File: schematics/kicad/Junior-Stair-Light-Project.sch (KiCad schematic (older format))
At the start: 72 parts, among them J1 12V Eingang, J2 LED_stripes_per_step, T1_1 BC337, T1_10 BC327, T1_11 BC337, T1_12 BC337, T1_13 BC337, T1_14 BC337, T1_15 BC337, T1_16 BC327, T1_17 BC327, T1_18 BC327, T1_19 BC327, T1_2 BC327, T1_20 BC327, T1_21 BC337, T1_22 BC337, T1_23 BC337, T1_24 BC327, T1_25 BC327, T1_26 BC327, T1_3 BC337, T1_4 BC337, T1_5 BC337, T1_6 BC337, T1_7 BC327, T1_8 BC327, T1_9 BC327, U1 7805, U2 Arduino_Nano

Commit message: First edition of PCB done
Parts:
- removed U1: 7805, symbol 7805
- added U1: L4940V5, TO_SOT_Packages_THT:TO-220_Vertical, symbol L4940V5
- C1, C2: footprint (none) -> Capacitors_THT:CP_Radial_D7.5mm_P2.50mm
- C3: footprint (none) -> Capacitors_THT:C_Disc_D3.8mm_W2.6mm_P2.50mm
- J1: footprint (none) -> Connectors_JST:JST_XH_B02B-XH-A_02x2.50mm_Straight
- J2: footprint (none) -> Connectors_JST:JST_XH_B15B-XH-A_15x2.50mm_Straight
- R10_1: renamed from R1_10; footprint (none) -> Resistors_THT:R_Axial_DIN0207_L6.3mm_D2.5mm_P7.62mm_Horizontal
- R10_2: renamed from R20; footprint (none) -> Resistors_THT:R_Axial_DIN0207_L6.3mm_D2.5mm_P7.62mm_Horizontal
- R10_3: renamed from R19; footprint (none) -> Resistors_THT:R_Axial_DIN0207_L6.3mm_D2.5mm_P7.62mm_Horizontal
- R11_1: renamed from R1_11; footprint (none) -> Resistors_THT:R_Axial_DIN0207_L6.3mm_D2.5mm_P7.62mm_Horizontal
- R11_2: renamed from R22; footprint (none) -> Resistors_THT:R_Axial_DIN0207_L6.3mm_D2.5mm_P7.62mm_Horizontal
- R11_3: renamed from R21; footprint (none) -> Resistors_THT:R_Axial_DIN0207_L6.3mm_D2.5mm_P7.62mm_Horizontal
- R12_1: renamed from R1_12; footprint (none) -> Resistors_THT:R_Axial_DIN0207_L6.3mm_D2.5mm_P7.62mm_Horizontal
- R12_2: renamed from R24; footprint (none) -> Resistors_THT:R_Axial_DIN0207_L6.3mm_D2.5mm_P7.62mm_Horizontal
- R12_3: renamed from R23; footprint (none) -> Resistors_THT:R_Axial_DIN0207_L6.3mm_D2.5mm_P7.62mm_Horizontal
- R13_1: renamed from R1_13; footprint (none) -> Resistors_THT:R_Axial_DIN0207_L6.3mm_D2.5mm_P7.62mm_Horizontal
- R13_2: renamed from R26; footprint (none) -> Resistors_THT:R_Axial_DIN0207_L6.3mm_D2.5mm_P7.62mm_Horizontal
- R13_3: renamed from R25; footprint (none) -> Resistors_THT:R_Axial_DIN0207_L6.3mm_D2.5mm_P7.62mm_Horizontal
- R1_1: footprint (none) -> Resistors_THT:R_Axial_DIN0207_L6.3mm_D2.5mm_P7.62mm_Horizontal
- R1_2: renamed from R2; footprint (none) -> Resistors_THT:R_Axial_DIN0207_L6.3mm_D2.5mm_P7.62mm_Horizontal
- R1_3: renamed from R1; footprint (none) -> Resistors_THT:R_Axial_DIN0207_L6.3mm_D2.5mm_P7.62mm_Horizontal
- R2_1: renamed from R1_2; footprint (none) -> Resistors_THT:R_Axial_DIN0207_L6.3mm_D2.5mm_P7.62mm_Horizontal
- R2_2: renamed from R4; footprint (none) -> Resistors_THT:R_Axial_DIN0207_L6.3mm_D2.5mm_P7.62mm_Horizontal
- R2_3: renamed from R3; footprint (none) -> Resistors_THT:R_Axial_DIN0207_L6.3mm_D2.5mm_P7.62mm_Horizontal
- R3_1: renamed from R1_3; footprint (none) -> Resistors_THT:R_Axial_DIN0207_L6.3mm_D2.5mm_P7.62mm_Horizontal
- R3_2: renamed from R6; footprint (none) -> Resistors_THT:R_Axial_DIN0207_L6.3mm_D2.5mm_P7.62mm_Horizontal
- R3_3: renamed from R5; footprint (none) -> Resistors_THT:R_Axial_DIN0207_L6.3mm_D2.5mm_P7.62mm_Horizontal
- R4_1: renamed from R1_4; footprint (none) -> Resistors_THT:R_Axial_DIN0207_L6.3mm_D2.5mm_P7.62mm_Horizontal
- R4_2: renamed from R8; footprint (none) -> Resistors_THT:R_Axial_DIN0207_L6.3mm_D2.5mm_P7.62mm_Horizontal
- R4_3: renamed from R7; footprint (none) -> Resistors_THT:R_Axial_DIN0207_L6.3mm_D2.5mm_P7.62mm_Horizontal
- R5_1: renamed from R1_5; footprint (none) -> Resistors_THT:R_Axial_DIN0207_L6.3mm_D2.5mm_P7.62mm_Horizontal
- R5_2: renamed from R10; footprint (none) -> Resistors_THT:R_Axial_DIN0207_L6.3mm_D2.5mm_P7.62mm_Horizontal
- R5_3: renamed from R9; footprint (none) -> Resistors_THT:R_Axial_DIN0207_L6.3mm_D2.5mm_P7.62mm_Horizontal
- R6_1: renamed from R1_6; footprint (none) -> Resistors_THT:R_Axial_DIN0207_L6.3mm_D2.5mm_P7.62mm_Horizontal
- R6_2: renamed from R12; footprint (none) -> Resistors_THT:R_Axial_DIN0207_L6.3mm_D2.5mm_P7.62mm_Horizontal
- R6_3: renamed from R11; footprint (none) -> Resistors_THT:R_Axial_DIN0207_L6.3mm_D2.5mm_P7.62mm_Horizontal
- R7_1: renamed from R1_7; footprint (none) -> Resistors_THT:R_Axial_DIN0207_L6.3mm_D2.5mm_P7.62mm_Horizontal
- R7_2: renamed from R14; footprint (none) -> Resistors_THT:R_Axial_DIN0207_L6.3mm_D2.5mm_P7.62mm_Horizontal
- R7_3: renamed from R13; footprint (none) -> Resistors_THT:R_Axial_DIN0207_L6.3mm_D2.5mm_P7.62mm_Horizontal
- R8_1: renamed from R1_8; footprint (none) -> Resistors_THT:R_Axial_DIN0207_L6.3mm_D2.5mm_P7.62mm_Horizontal
- R8_2: renamed from R16; footprint (none) -> Resistors_THT:R_Axial_DIN0207_L6.3mm_D2.5mm_P7.62mm_Horizontal
- R8_3: renamed from R15; footprint (none) -> Resistors_THT:R_Axial_DIN0207_L6.3mm_D2.5mm_P7.62mm_Horizontal
- R9_1: renamed from R1_9; footprint (none) -> Resistors_THT:R_Axial_DIN0207_L6.3mm_D2.5mm_P7.62mm_Horizontal
- R9_2: renamed from R18; footprint (none) -> Resistors_THT:R_Axial_DIN0207_L6.3mm_D2.5mm_P7.62mm_Horizontal
- R9_3: renamed from R17; footprint (none) -> Resistors_THT:R_Axial_DIN0207_L6.3mm_D2.5mm_P7.62mm_Horizontal
- T1_1, T1_10, T1_11, T1_12, T1_13, T1_14, T1_15, T1_16, T1_17, T1_18, T1_19, T1_2, T1_20, T1_21, T1_22, T1_23, T1_24, T1_25, T1_26, T1_3, T1_4, T1_5, T1_6, T1_7, T1_8, T1_9: footprint (none) -> TO_SOT_Packages_THT:TO-92_Inline_Narrow_Oval
- U2: footprint (none) -> NOKO_Wetimer:Arduino_Nano
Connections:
- wire segments 203 -> 202
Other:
- moved on the sheet: C1, C2, C3, J1

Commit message: Some changes
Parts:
- added J? (x2): CONN_01X03, symbol CONN_01X03
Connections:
- net +5V: now also J?.1 (P1), J?.1 (P1)
- net GND: now also J?.3 (P3), J?.3 (P3)
- net Step12_a: now also U2.16 (D13); no longer U2.19 (A0)
- net Step13_a: now also U2.19 (A0); no longer U2.20 (A1)
- net IR_2: now reaches U2.25 (A6)
- net IR_2: now also J?.2 (P2)
- net IR_1: now reaches U2.26 (A7)
- net IR_1: now also J?.2 (P2)
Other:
- moved on the sheet: J2, R10_1, R10_2, R10_3, R11_1, R11_2, R11_3, R12_1, R12_2, R12_3, R13_1, R13_2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

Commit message: First RC of code is ready
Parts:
- added 100k: R, symbol R
- added R?: 100k, symbol R
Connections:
- net +5V: now also 100k.1, R?.1
- net at U2.27 (5V): now also J?.2 (P2), 100k.2
- net IR_1: no longer names the net of U2.26 (A7)
- net IR_1: now also J?.2 (P2), R?.2; no longer J?.2 (P2)
- net IR_2: no longer names the net of U2.25 (A6)
- net IR_2: no longer J?.2 (P2)
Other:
- note added: "To the positive lines of the LED stripes.\nAll GND lines are connected to GND\ndirectly."
- note removed: "Zu den Pluspolen der LED Streifen.\nMasse der LED Streifen sind alle an\nMasse angeschlossen."
- moved on the sheet: C1, C2, C3, J1, J?, U1, U2

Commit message: Changes
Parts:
- R1: renamed from 100k; value R -> 10k
- R2: renamed from R?; value 100k -> 10k
- gave numbers to parts that had none: 2
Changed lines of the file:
@@
 $EndComp
 $Comp
-L +12V #PWR01
+L +12V #PWR4
 U 1 1 5AC3BE82
 P 6375 850
-F 0 "#PWR01" H 6375 700 50  0001 C CNN
+F 0 "#PWR4" H 6375 700 50  0001 C CNN
 F 1 "+12V" H 6375 990 50  0000 C CNN
 F 2 "" H 6375 850 50  0001 C CNN
@@
 $EndComp
 $Comp
-L GND #PWR02
+L GND #PWR5
 U 1 1 5AC3BF02
 P 6375 2450
-F 0 "#PWR02" H 6375 2200 50  0001 C CNN
+F 0 "#PWR5" H 6375 2200 50  0001 C CNN
 F 1 "GND" H 6375 2300 50  0000 C CNN
 F 2 "" H 6375 2450 50  0001 C CNN
@@
 $EndComp
 $Comp
-L GND #PWR03
+L GND #PWR6
 U 1 1 5AC3BFE4
 P 7125 2450
-F 0 "#PWR03" H 7125 2200 50  0001 C CNN
+F 0 "#PWR6" H 7125 2200 50  0001 C CNN
 F 1 "GND" H 7125 2300 50  0000 C CNN
 F 2 "" H 7125 2450 50  0001 C CNN
@@
 $EndComp
 $Comp
-L +5V #PWR04
+L +5V #PWR8
 U 1 1 5AC3C27B
 P 7975 850
-F 0 "#PWR04" H 7975 700 50  0001 C CNN
+F 0 "#PWR8" H 7975 700 50  0001 C CNN
 F 1 "+5V" H 7975 990 50  0000 C CNN
 F 2 "" H 7975 850 50  0001 C CNN
@@
 $EndComp
 $Comp
-L +5V #PWR05
+L +5V #PWR7
 U 1 1 5AC3C2F8
 P 7925 3450
-F 0 "#PWR05" H 7925 3300 50  0001 C CNN
+F 0 "#PWR7" H 7925 3300 50  0001 C CNN
 F 1 "+5V" H 7925 3590 50  0000 C CNN
 F 2 "" H 7925 3450 50  0001 C CNN
@@
 $EndComp
 $Comp
-L GND #PWR06
+L GND #PWR9
 U 1 1 5AC3C334
 P 8025 5450
-F 0 "#PWR06" H 8025 5200 50  0001 C CNN
+F 0 "#PWR9" H 8025 5200 50  0001 C CNN
 F 1 "GND" H 8025 5300 50  0000 C CNN
 F 2 "" H 8025 5450 50  0001 C CNN
@@
 	1175 1875 1175 7025
 $Comp
-L GND #PWR08
+L GND #PWR1
 U 1 1 5AD4FE78
 P 1175 7025
-F 0 "#PWR08" H 1175 6775 50  0001 C CNN
+F 0 "#PWR1" H 1175 6775 50  0001 C CNN
 F 1 "GND" H 1175 6875 50  0000 C CNN
 F 2 "" H 1175 7025 50  0001 C CNN
@@
 	2900 1875 2900 7025
 $Comp
-L GND #PWR09
+L GND #PWR2
 U 1 1 5AD51A90
 P 2900 7025
-F 0 "#PWR09" H 2900 6775 50  0001 C CNN
+F 0 "#PWR2" H 2900 6775 50  0001 C CNN
 F 1 "GND" H 2900 6875 50  0000 C CNN
 F 2 "" H 2900 7025 50  0001 C CNN
@@
 	4625 1875 4625 4575
 $Comp
-L GND #PWR010
+L GND #PWR3
 U 1 1 5AD543C0
 P 4625 4575
-F 0 "#PWR010" H 4625 4325 50  0001 C CNN
+F 0 "#PWR3" H 4625 4325 50  0001 C CNN
 F 1 "GND" H 4625 4425 50  0000 C CNN
 F 2 "" H 4625 4575 50  0001 C CNN
@@
 	9800 4950 9800 4800
 $Comp
-L CONN_01X03 J?
+L CONN_01X03 J3
 U 1 1 5AE78337
 P 9900 2950
-F 0 "J?" H 9900 3150 50  0000 C CNN
+F 0 "J3" H 9900 3150 50  0000 C CNN
 F 1 "CONN_01X03" V 10000 2950 50  0000 C CNN
 F 2 "" H 9900 2950 50  0001 C CNN
@@
 $EndComp
 $Comp
-L CONN_01X03 J?
+L CONN_01X03 J4
 U 1 1 5AE7844B
 P 9900 3500
-F 0 "J?" H 9900 3700 50  0000 C CNN
+F 0 "J4" H 9900 3700 50  0000 C CNN
 F 1 "CONN_01X03" V 10000 3500 50  0000 C CNN
 F 2 "" H 9900 3500 50  0001 C CNN
@@
 $EndComp
 $Comp
-L GND #PWR?
+L GND #PWR12
 U 1 1 5AE78EBA
 P 9250 4450
-F 0 "#PWR?" H 9250 4200 50  0001 C CNN
+F 0 "#PWR12" H 9250 4200 50  0001 C CNN
 F 1 "GND" H 9250 4300 50  0000 C CNN
 F 2 "" H 9250 4450 50  0001 C CNN
@@
 $EndComp
 $Comp
-L R 100k
+L R R1
 U 1 1 5B89507E
 P 8225 3700
-F 0 "100k" V 8305 3700 50  0000 C CNN
-F 1 "R" V 8225 3700 50  0000 C CNN
+F 0 "R1" V 8305 3700 50  0000 C CNN
+F 1 "10k" V 8225 3700 50  0000 C CNN
 F 2 "" V 8155 3700 50  0001 C CNN
 F 3 "" H 8225 3700 50  0001 C CNN
@@
 Connection ~ 9250 3600
 $Comp
-L +5V #PWR?
+L +5V #PWR13
 U 1 1 5B8988D6
 P 9450 2650
-F 0 "#PWR?" H 9450 2500 50  0001 C CNN
+F 0 "#PWR13" H 9450 2500 50  0001 C CNN
 F 1 "+5V" H 9450 2790 50  0000 C CNN
 F 2 "" H 9450 2650 50  0001 C CNN
@@
 	8700 3950 7525 3950
 $Comp
-L +5V #PWR?
+L +5V #PWR10
 U 1 1 5B89A2E0
 P 8225 3450
-F 0 "#PWR?" H 8225 3300 50  0001 C CNN
+F 0 "#PWR10" H 8225 3300 50  0001 C CNN
 F 1 "+5V" H 8225 3590 50  0000 C CNN
 F 2 "" H 8225 3450 50  0001 C CNN
@@
 $EndComp
 $Comp
-L +5V #PWR?
+L +5V #PWR11
 U 1 1 5B89A848
 P 8425 3450
-F 0 "#PWR?" H 8425 3300 50  0001 C CNN
+F 0 "#PWR11" H 8425 3300 50  0001 C CNN
 F 1 "+5V" H 8425 3590 50  0000 C CNN
 F 2 "" H 8425 3450 50  0001 C CNN
@@
 $EndComp
 $Comp
-L R R?
+L R R2
 U 1 1 5B89A934
 P 8425 3700
-F 0 "R?" V 8505 3700 50  0000 C CNN
-F 1 "100k" V 8425 3700 50  0000 C CNN
+F 0 "R2" V 8505 3700 50  0000 C CNN
+F 1 "10k" V 8425 3700 50  0000 C CNN
 F 2 "" V 8355 3700 50  0001 C CNN
 F 3 "" H 8425 3700 50  0001 C CNN

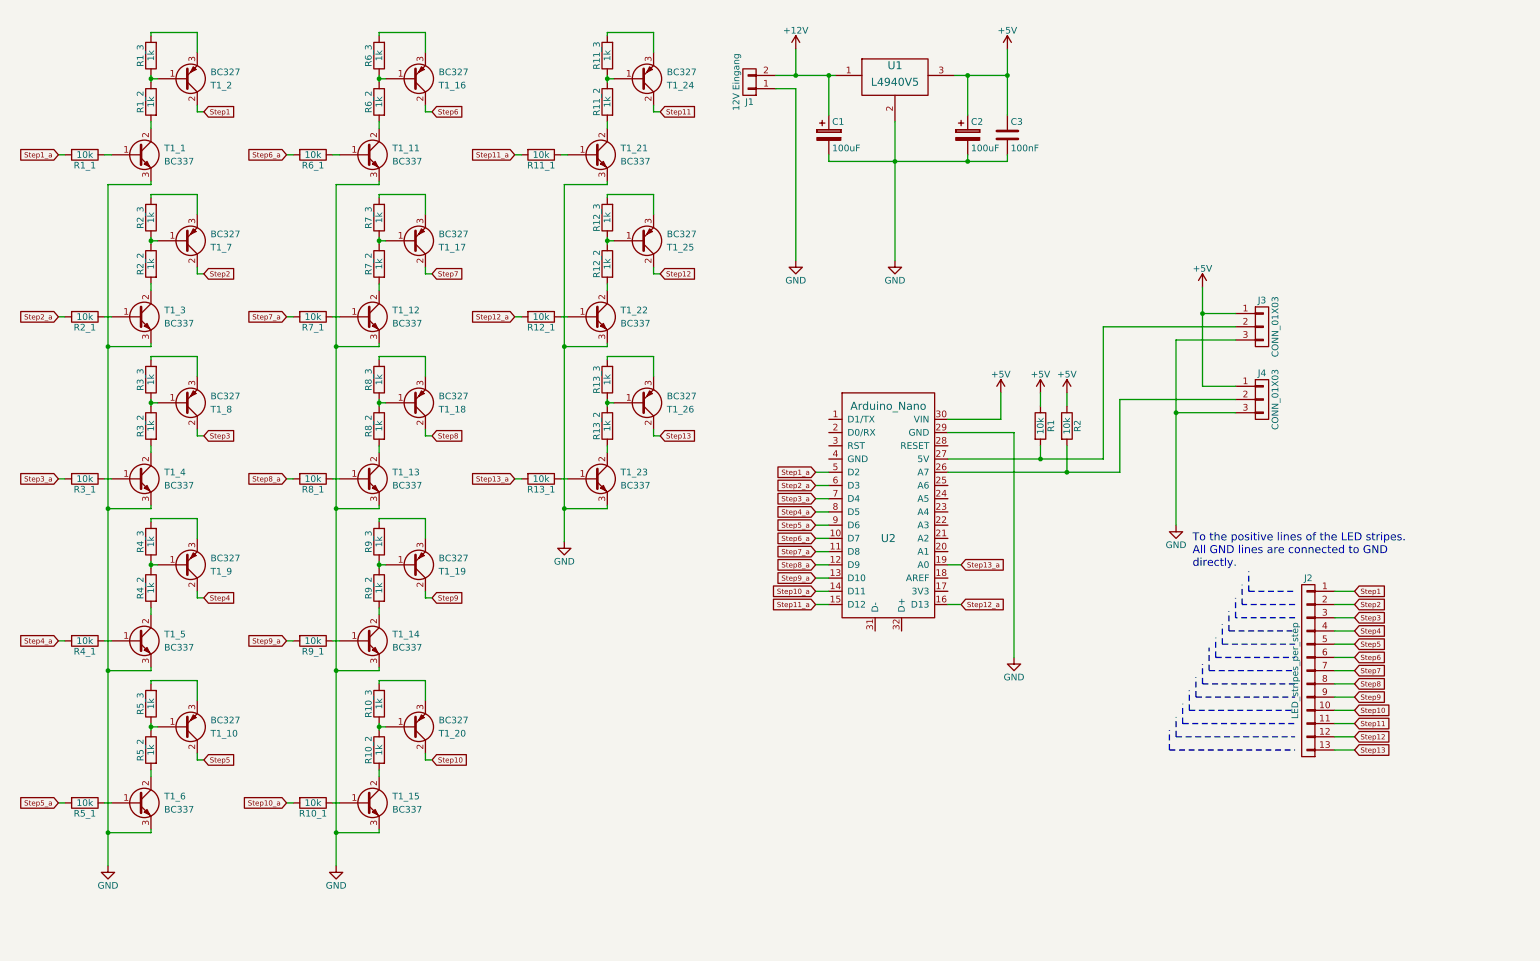
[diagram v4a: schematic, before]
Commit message: Added max channels (19) and finished first RC of PCB layout
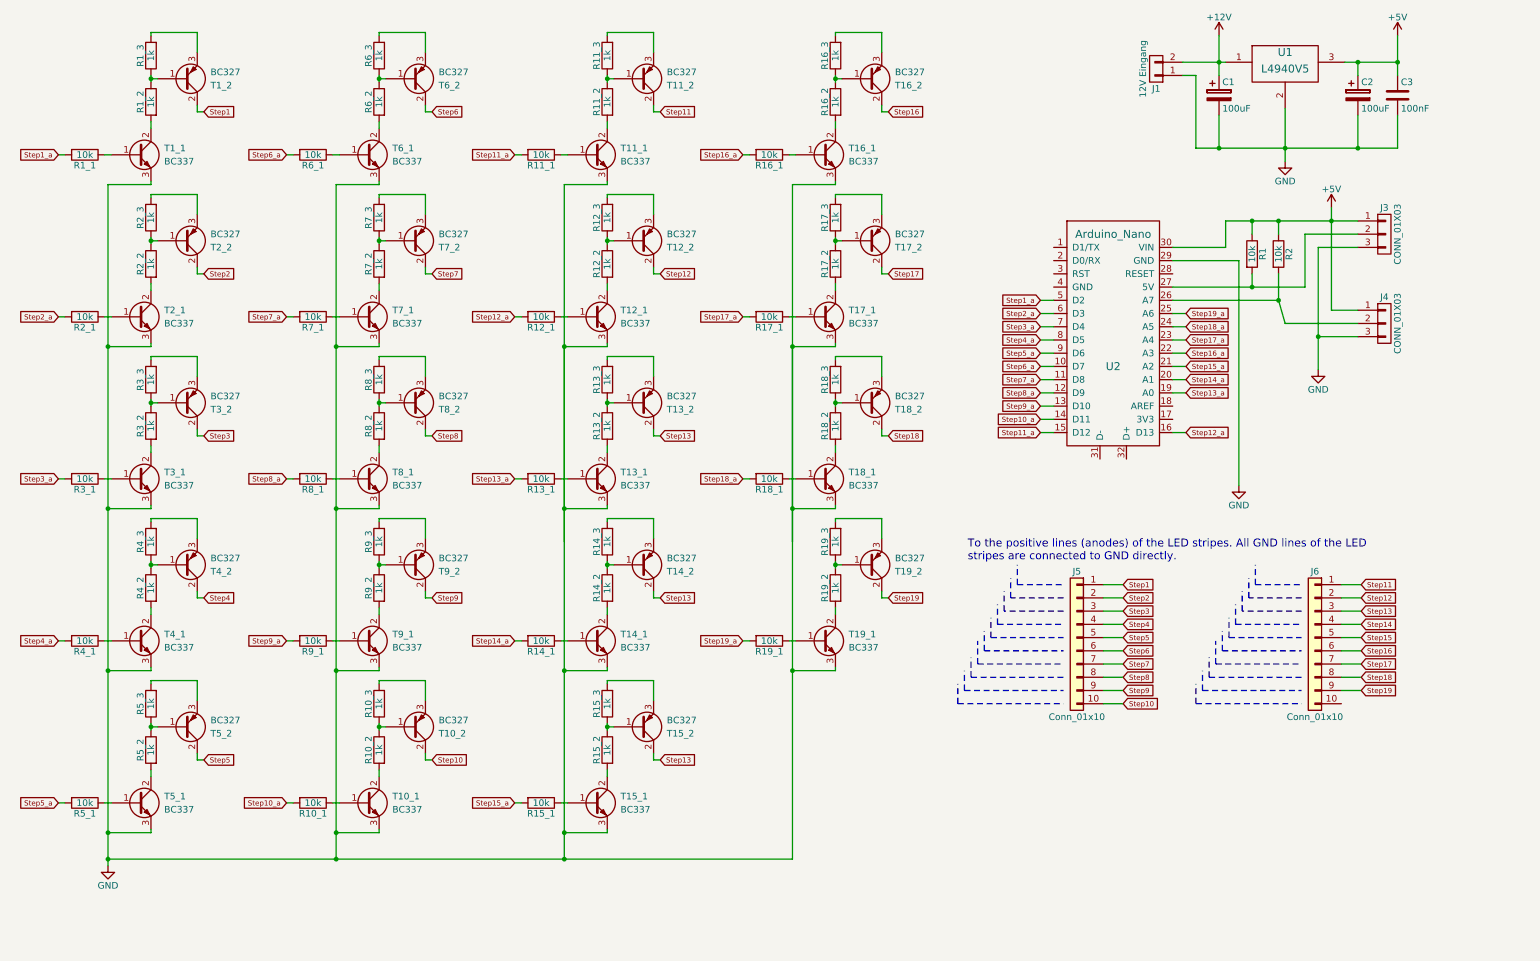
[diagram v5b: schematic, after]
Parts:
- removed J2: LED_stripes_per_step, Connectors_JST:JST_XH_B15B-XH-A_15x2.50mm_Straight, symbol CONN_01X13
- added J5, J6: Conn_01x10, Connectors_JST:JST_XH_B10B-XH-A_10x2.50mm_Straight, symbol Conn_01x10
- added R14_1, R15_1, R16_1, R17_1, R18_1, R19_1: 10k, Resistors_THT:R_Axial_DIN0207_L6.3mm_D2.5mm_P7.62mm_Horizontal, symbol R
- added R14_2, R14_3, R15_2, R15_3, R16_2, R16_3, R17_2, R17_3, R18_2, R18_3, R19_2, R19_3: 1k, Resistors_THT:R_Axial_DIN0207_L6.3mm_D2.5mm_P7.62mm_Horizontal, symbol R
- added T14_1, T15_1, T16_1, T17_1, T18_1, T19_1: BC337, TO_SOT_Packages_THT:TO-92_Inline_Narrow_Oval, symbol Q_NPN_BCE
- added T14_2, T15_2, T16_2, T17_2, T18_2, T19_2: BC327, TO_SOT_Packages_THT:TO-92_Inline_Narrow_Oval, symbol Q_PNP_BCE
- J3, J4: footprint (none) -> Connectors_JST:JST_XH_B03B-XH-A_03x2.50mm_Straight
- R1, R2: footprint (none) -> Resistors_THT:R_Axial_DIN0207_L6.3mm_D2.5mm_P7.62mm_Horizontal
- renumbered T1_15 to T10_1, T1_20 to T10_2, T1_21 to T11_1, T1_24 to T11_2, T1_22 to T12_1, T1_25 to T12_2, T1_23 to T13_1, T1_26 to T13_2, T1_3 to T2_1, T1_7 to T2_2, T1_4 to T3_1, T1_8 to T3_2, T1_5 to T4_1, T1_9 to T4_2, T1_6 to T5_1, T1_10 to T5_2, T1_11 to T6_1, T1_16 to T6_2, T1_12 to T7_1, T1_17 to T7_2, T1_13 to T8_1, T1_18 to T8_2, T1_14 to T9_1, T1_19 to T9_2
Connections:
- net GND: now also T14_1.3 (E), T15_1.3 (E), T16_1.3 (E), T17_1.3 (E), T18_1.3 (E), T19_1.3 (E)
- net Step1: now also J5.1 (Pin_1)
- net Step10: now also J5.10 (Pin_10)
- net Step11: now also J6.1 (Pin_1)
- net Step12: now also J6.2 (Pin_2)
- net Step13: now also J6.3 (Pin_3), T14_2.2 (C), T15_2.2 (C)
- net Step2: now also J5.2 (Pin_2)
- net Step3: now also J5.3 (Pin_3)
- net Step4: now also J5.4 (Pin_4)
- net Step5: now also J5.5 (Pin_5)
- net Step6: now also J5.6 (Pin_6)
- net Step7: now also J5.7 (Pin_7)
- net Step8: now also J5.8 (Pin_8)
- net Step9: now also J5.9 (Pin_9)
- net Step14_a: now reaches U2.20 (A1)
- net Step14_a: now also R14_1.2
- net Step15_a: now reaches U2.21 (A2)
- net Step15_a: now also R15_1.2
- net Step16_a: now reaches U2.22 (A3)
- net Step16_a: now also R16_1.2
- net Step17_a: now reaches U2.23 (A4)
- net Step17_a: now also R17_1.2
- net Step18_a: now reaches U2.24 (A5)
- net Step18_a: now also R18_1.2
- net Step19_a: now reaches U2.25 (A6)
- net Step19_a: now also R19_1.2
- new net: R14_1.1, T14_1.1 (B)
- new net: R14_2.2, T14_1.2 (C)
- new net: R14_2.1, R14_3.1, T14_2.1 (B)
- new net: R14_3.2, T14_2.3 (E)
- new net: R15_1.1, T15_1.1 (B)
- new net: R15_2.2, T15_1.2 (C)
- new net: R15_2.1, R15_3.1, T15_2.1 (B)
- new net: R15_3.2, T15_2.3 (E)
- new net: R16_1.1, T16_1.1 (B)
- new net: R16_2.2, T16_1.2 (C)
- new net: R16_2.1, R16_3.1, T16_2.1 (B)
- new net: R16_3.2, T16_2.3 (E)
- new net: R17_1.1, T17_1.1 (B)
- new net: R17_2.2, T17_1.2 (C)
- new net: R17_2.1, R17_3.1, T17_2.1 (B)
- new net: R17_3.2, T17_2.3 (E)
- new net: R18_1.1, T18_1.1 (B)
- new net: R18_2.2, T18_1.2 (C)
- new net: R18_2.1, R18_3.1, T18_2.1 (B)
- new net: R18_3.2, T18_2.3 (E)
- new net: R19_1.1, T19_1.1 (B)
- new net: R19_2.2, T19_1.2 (C)
- new net: R19_2.1, R19_3.1, T19_2.1 (B)
- new net: R19_3.2, T19_2.3 (E)
- new net Step14: J6.4 (Pin_4)
- new net Step15: J6.5 (Pin_5)
- new net Step16: J6.6 (Pin_6), T16_2.2 (C)
- new net Step17: J6.7 (Pin_7), T17_2.2 (C)
- new net Step18: J6.8 (Pin_8), T18_2.2 (C)
- new net Step19: J6.9 (Pin_9), T19_2.2 (C)
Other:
- note added: "To the positive lines (anodes) of the LED stripes. All GND lines of the LED\nstripes are connected to GND directly."
- note removed: "To the positive lines of the LED stripes.\nAll GND lines are connected to GND\ndirectly."
- moved on the sheet: C1, C2, C3, J1, J3, J4, R1, R2, U1, U2
